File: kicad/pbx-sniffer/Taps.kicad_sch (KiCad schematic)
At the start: 1 part, among them U3 Optocoupler_DC_PhotoNPN_AKEC

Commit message: add footprints and part numbers for power caps
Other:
- company: (none) -> M5
- title: (none) -> Telethon PBX Sniffer
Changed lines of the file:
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@@
 	(generator_version "9.0")
 	(paper "A4")
+	(title_block
+		(title "Telethon PBX Sniffer")
+		(date "2026-02-03")
+		(rev "v0.1")
+		(company "M5")
+		(comment 4 "Tobe Cynar, Ian Butler")
+		(comment 5 "Ian Butler")
+	)
 	(text "differential voltage tracker, when voltage is <7, ADC is connected, else disconnected. control signal can on/off hook line."
 		(exclude_from_sim no)

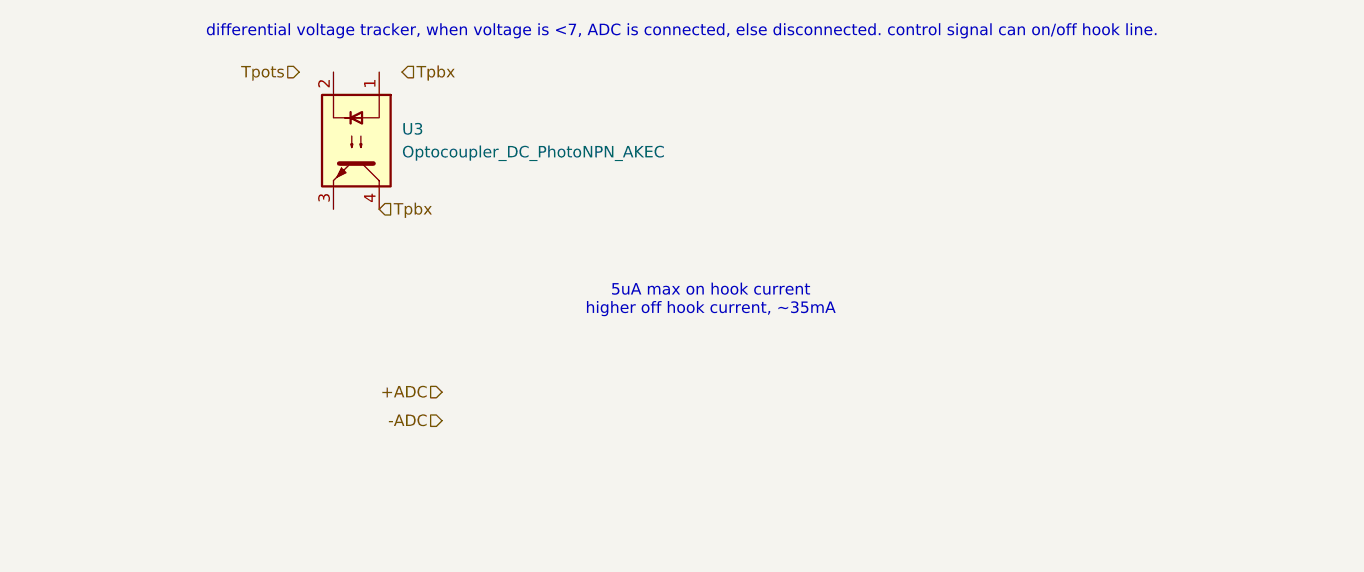
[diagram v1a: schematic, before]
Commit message: updated annotation on wiretap board
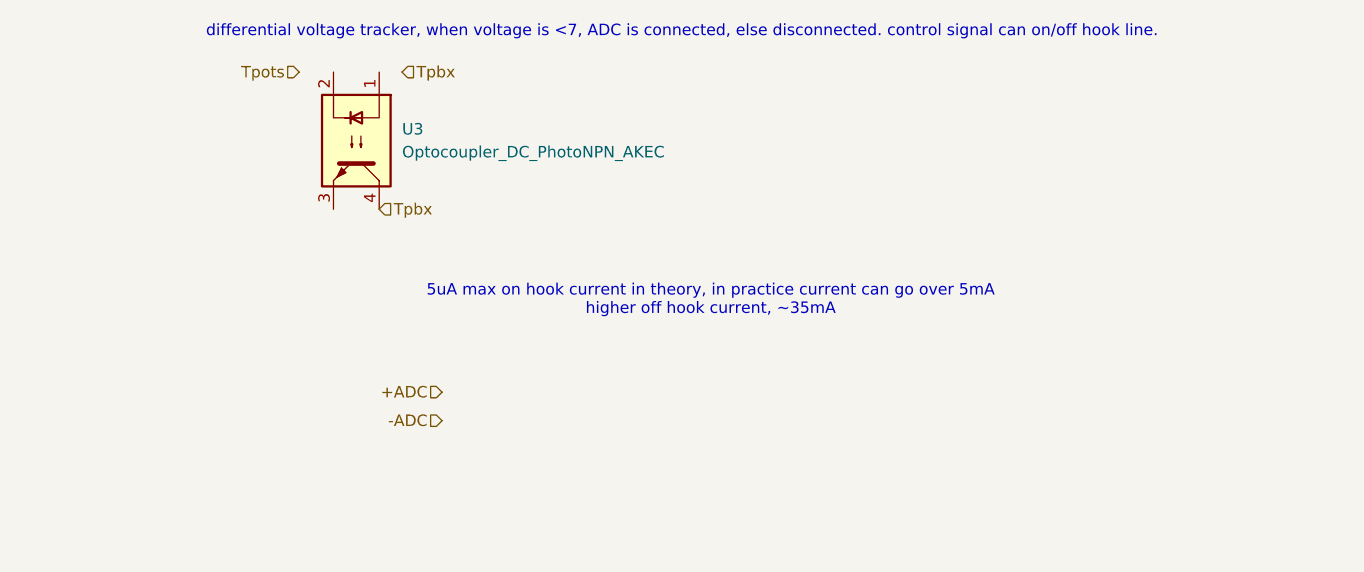
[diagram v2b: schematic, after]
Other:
- note added: "5uA max on hook current in theory, in practice current can go over 5mA higher off hook current, ~35mA"
- note removed: "5uA max on hook current higher off hook current, ~35mA"
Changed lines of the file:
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@@
 		)
 	)
-	(text "5uA max on hook current\nhigher off hook current, ~35mA"
+	(text "5uA max on hook current in theory, in practice current can go over 5mA\nhigher off hook current, ~35mA"
 		(exclude_from_sim no)
 		(at 83.185 46.99 0)

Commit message: added relays and wiretap circuits to schematic
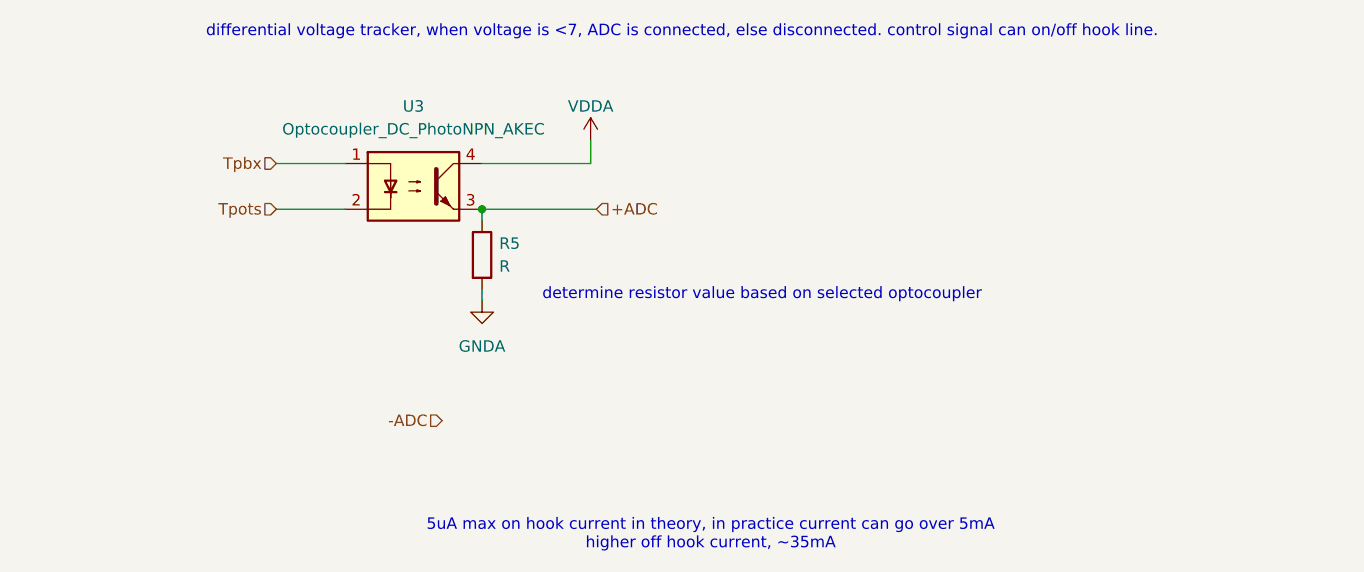
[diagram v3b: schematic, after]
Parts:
- added R5: R, symbol Device:R
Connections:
- net +ADC: now also U3.3, R5.1
- net Tpbx: now also U3.1; no longer U3.4
- net Tpots: now also U3.2
- new net GNDA: R5.2
- new net VDDA: U3.4
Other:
- note added: "determine resistor value based on selected optocoupler"
- moved on the sheet: U3

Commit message: working on duplicating adc and control circuits between phone jacks
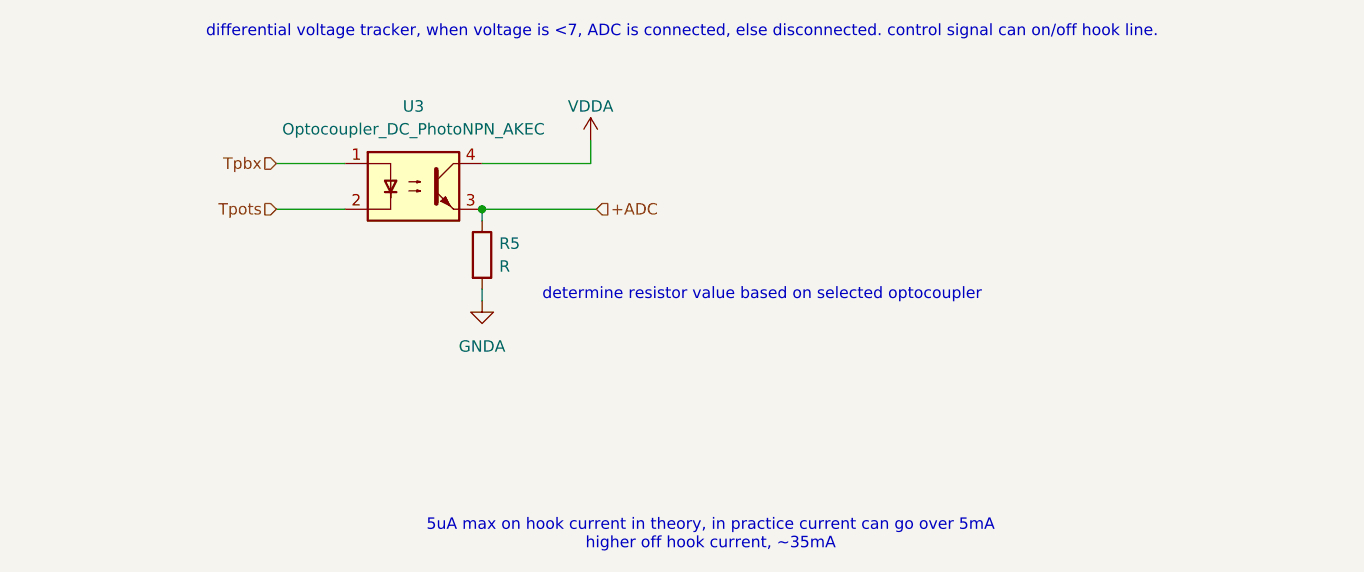
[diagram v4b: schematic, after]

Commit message: assigned footprints, added components to pcb
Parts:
- R5: footprint (none) -> Resistor_THT:R_Axial_DIN0207_L6.3mm_D2.5mm_P10.16mm_Horizontal
- U3: footprint (none) -> Package_DIP:DIP-4_W7.62mm_LongPads
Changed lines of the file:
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@@
 			)
 		)
-		(property "Footprint" ""
+		(property "Footprint" "Package_DIP:DIP-4_W7.62mm_LongPads"
 			(at 45.085 39.37 0)
 			(effects
@@
 			)
 		)
-		(property "Footprint" ""
+		(property "Footprint" "Resistor_THT:R_Axial_DIN0207_L6.3mm_D2.5mm_P10.16mm_Horizontal"
 			(at 56.007 41.91 90)
 			(effects

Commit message: commenced placement on pcb
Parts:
- added JP1: JUP_P10mm, PCM_SL_Jumpers:JUP_P10mm, symbol PCM_SL_Jumpers_THT:JUP_P10mm
- renumbered R5 to R2
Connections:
- net Tpbx: now also JP1.2
- net Tpots: now also JP1.1

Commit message: add part numbers for remaining important parts
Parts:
- U3: DKPN (none) -> 559-PS2565L1-1Y-A-ND
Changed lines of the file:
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@@
+			)
+		)
+		(property "DKPN" "559-PS2565L1-1Y-A-ND"
+			(at 50.165 34.29 0)
+			(effects
+				(font
+					(size 1.27 1.27)
+				)
+				(hide yes)
 			)
 		)

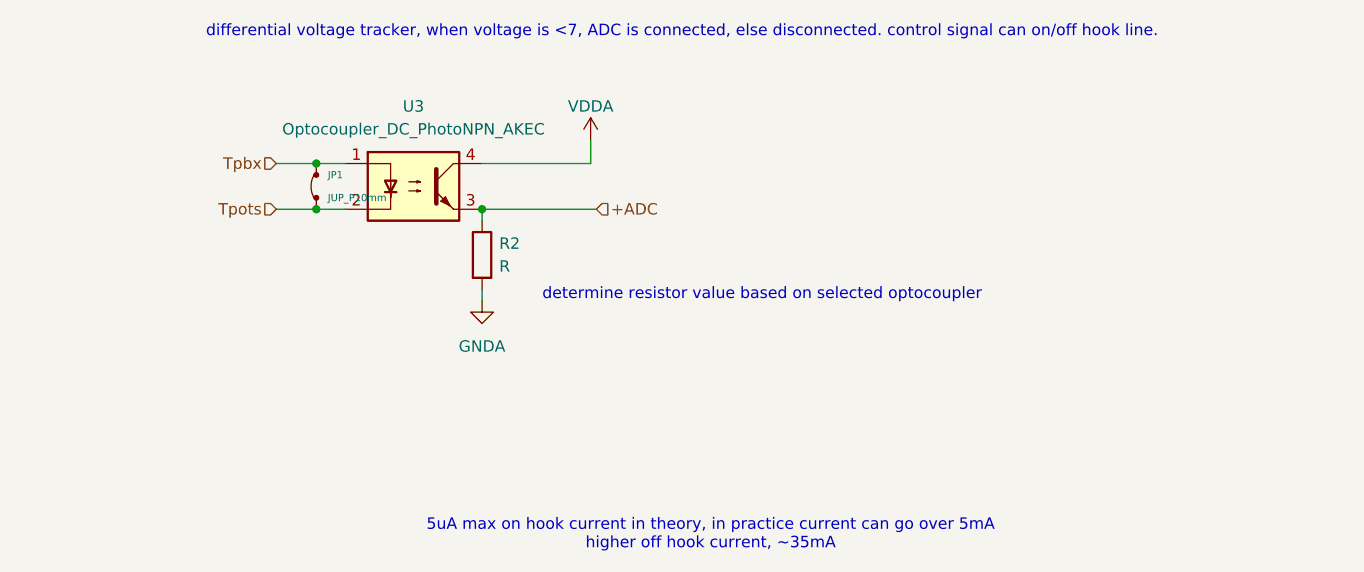
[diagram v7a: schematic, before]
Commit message: redid wiring in order to make power planes doable
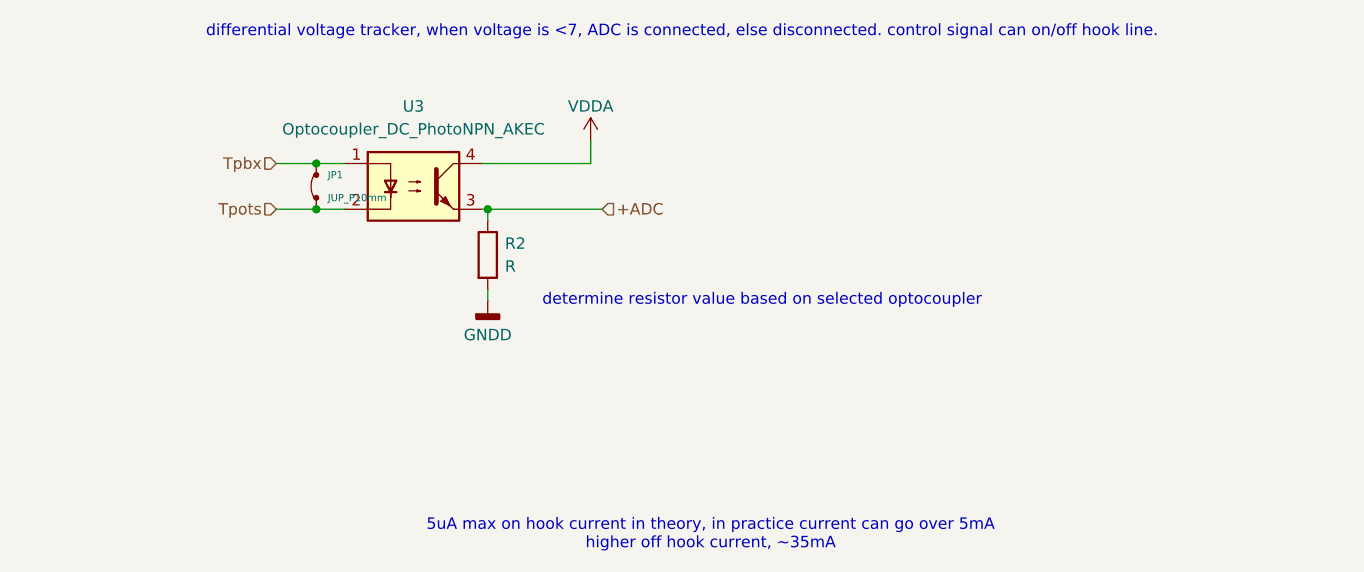
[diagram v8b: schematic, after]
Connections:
- net GNDA renamed GNDD
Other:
- moved on the sheet: R2
